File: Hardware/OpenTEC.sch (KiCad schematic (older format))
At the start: 52 parts

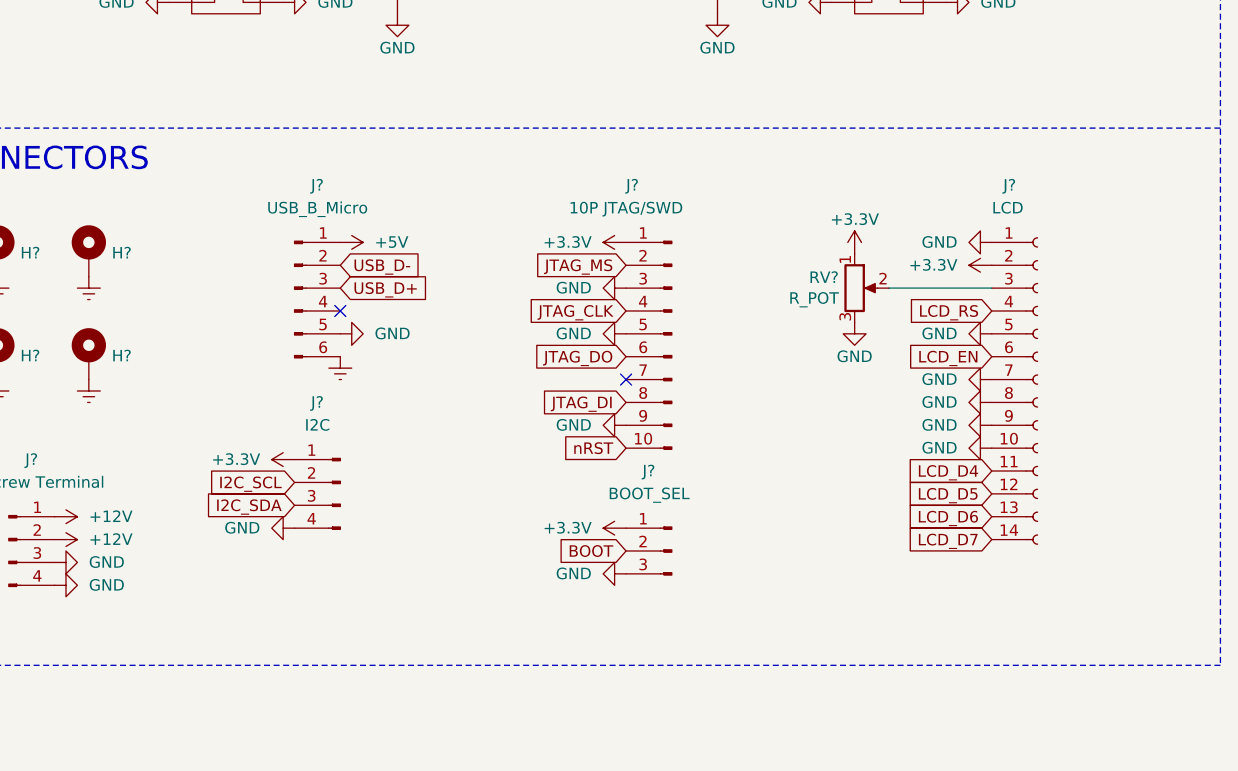
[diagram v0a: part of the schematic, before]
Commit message: Add temperature sensor connectors
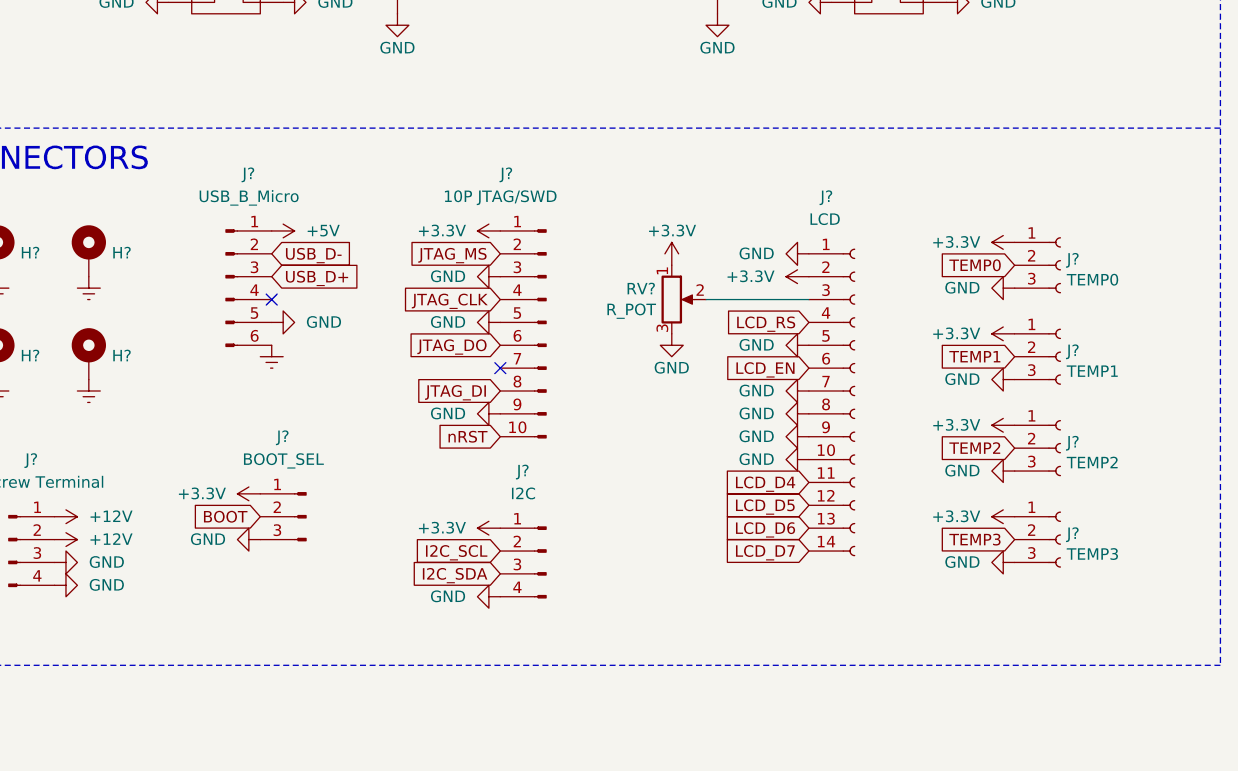
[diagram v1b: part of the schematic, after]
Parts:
- added J?: TEMP0, symbol Connector:Conn_01x03_Female
- added J?: TEMP1, symbol Connector:Conn_01x03_Female
- added J?: TEMP2, symbol Connector:Conn_01x03_Female
- added J?: TEMP3, symbol Connector:Conn_01x03_Female
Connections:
- net +3V3: now also J?.1 (Pin_1), J?.1 (Pin_1), J?.1 (Pin_1), J?.1 (Pin_1)
- net GND: now also J?.3 (Pin_3), J?.3 (Pin_3), J?.3 (Pin_3), J?.3 (Pin_3)
- net TEMP0: now also J?.2 (Pin_2)
- net TEMP1: now also J?.2 (Pin_2)
- net TEMP2: now also J?.2 (Pin_2)
- net TEMP3: now also J?.2 (Pin_2)
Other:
- moved on the sheet: J?, RV?

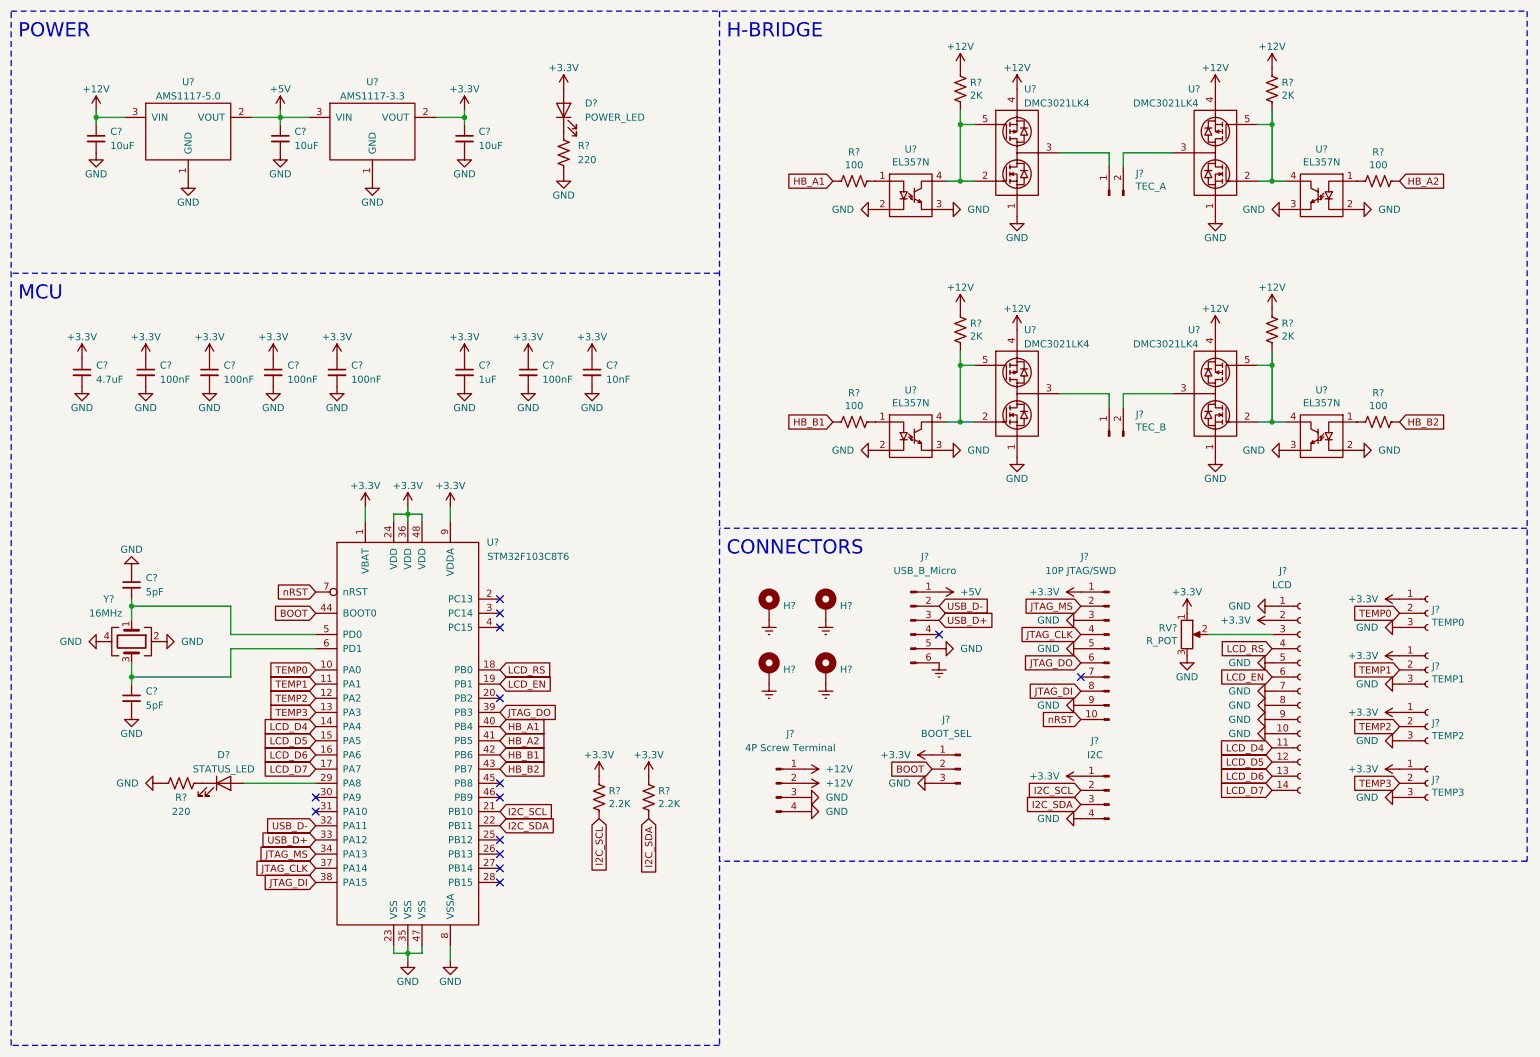
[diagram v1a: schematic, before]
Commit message: Add fan headers
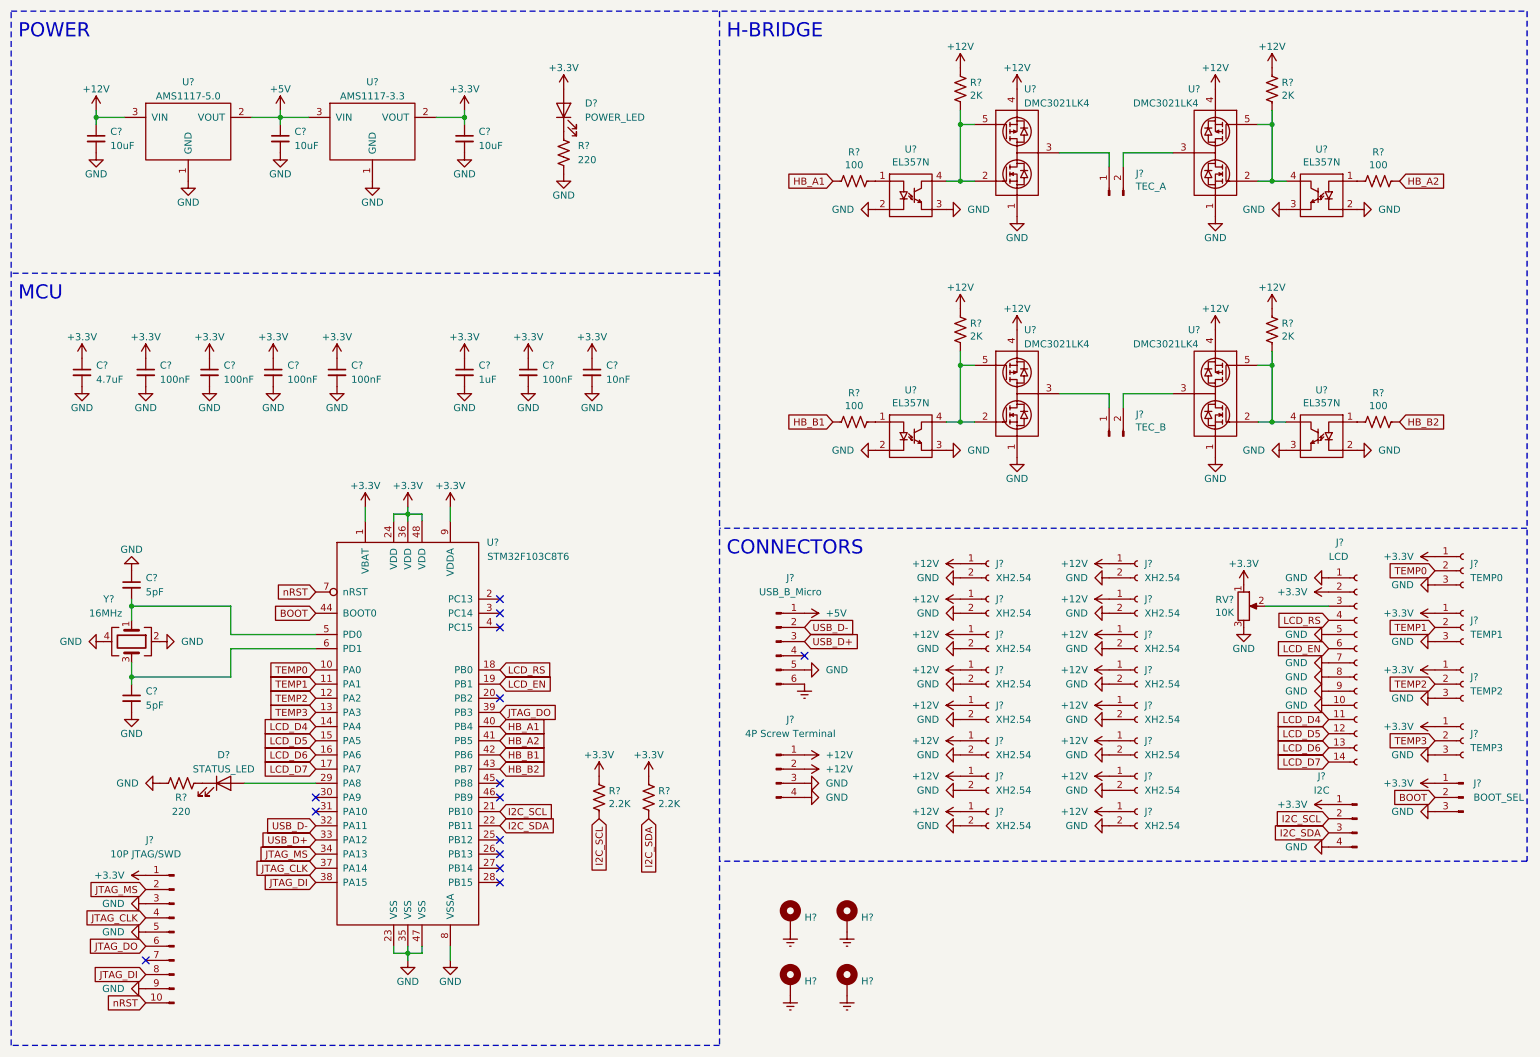
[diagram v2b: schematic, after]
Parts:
- added J? (x16): XH2.54, symbol Connector:Conn_01x02_Female
- RV?: value R_POT -> 10K
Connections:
- net +12V: now also J?.1 (Pin_1), J?.1 (Pin_1), J?.1 (Pin_1), J?.1 (Pin_1), J?.1 (Pin_1), J?.1 (Pin_1), J?.1 (Pin_1), J?.1 (Pin_1), J?.1 (Pin_1), J?.1 (Pin_1), J?.1 (Pin_1), J?.1 (Pin_1), J?.1 (Pin_1), J?.1 (Pin_1), J?.1 (Pin_1), J?.1 (Pin_1)
- net GND: now also J?.2 (Pin_2), J?.2 (Pin_2), J?.2 (Pin_2), J?.2 (Pin_2), J?.2 (Pin_2), J?.2 (Pin_2), J?.2 (Pin_2), J?.2 (Pin_2), J?.2 (Pin_2), J?.2 (Pin_2), J?.2 (Pin_2), J?.2 (Pin_2), J?.2 (Pin_2), J?.2 (Pin_2), J?.2 (Pin_2), J?.2 (Pin_2)
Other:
- moved on the sheet: H?, J?, RV?

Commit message: Add footprints to components
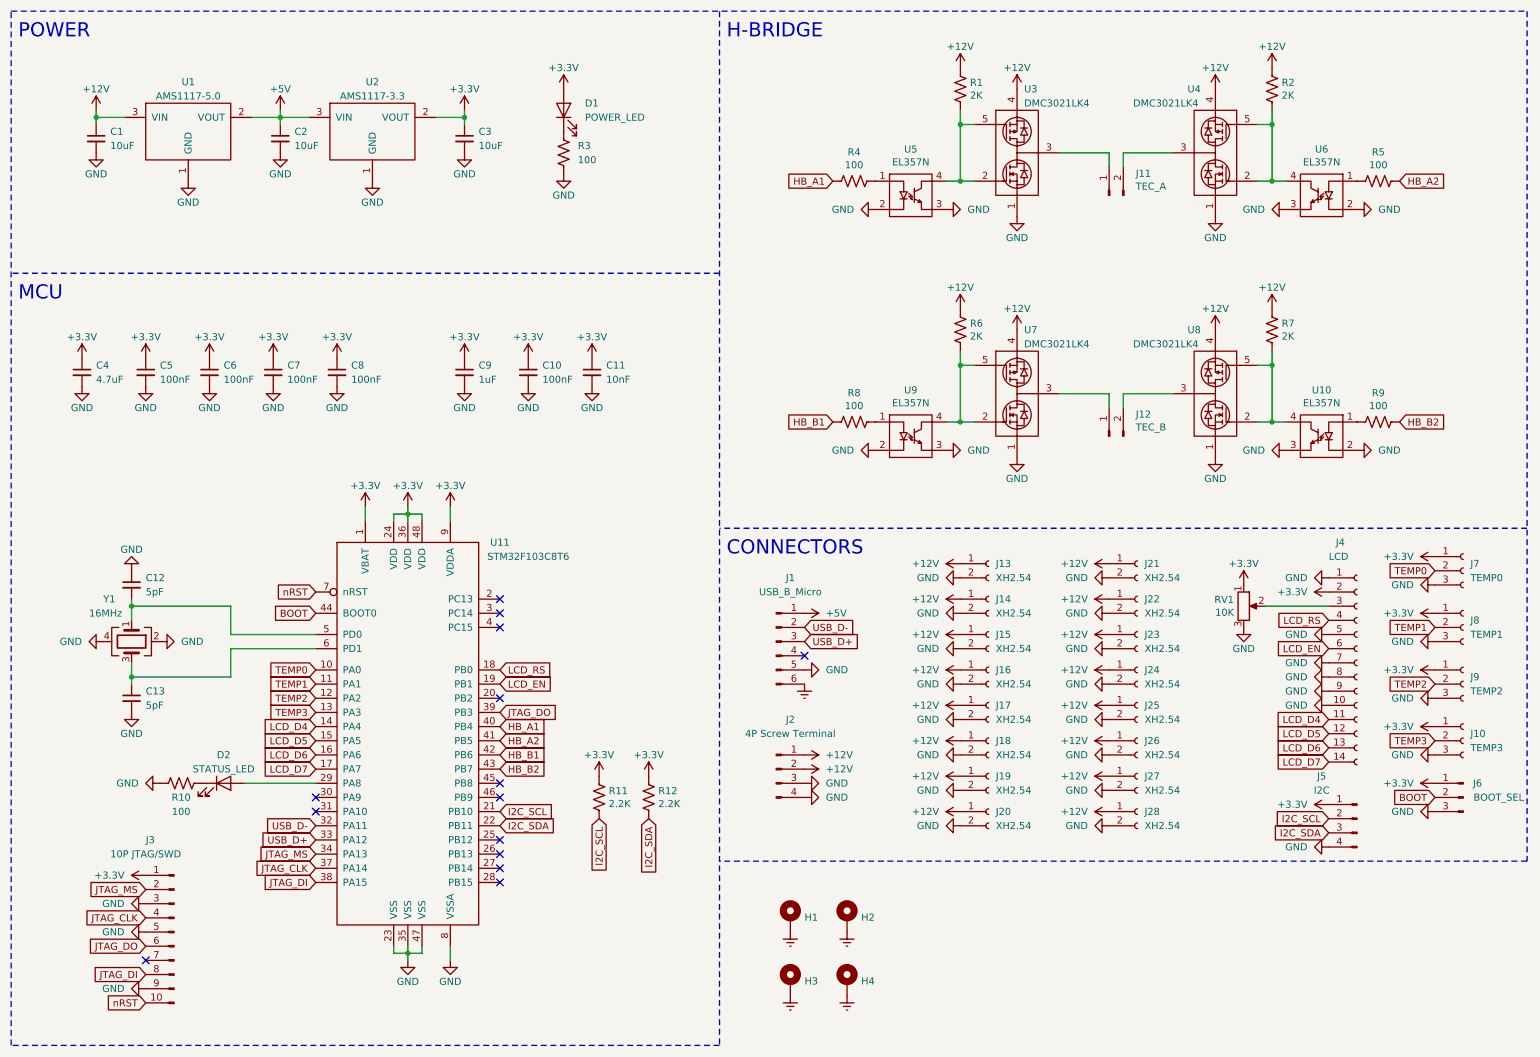
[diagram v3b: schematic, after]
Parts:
- C1, C2, C3, C4, C9: renamed from C?; footprint (none) -> Capacitor_SMD:C_0805_2012Metric
- C10, C11, C5, C6, C7, C8: renamed from C?; footprint (none) -> Capacitor_SMD:C_0402_1005Metric
- C12, C13: renamed from C?; footprint (none) -> Capacitor_SMD:C_0603_1608Metric
- D1, D2: renamed from D?; footprint (none) -> LED_SMD:LED_0603_1608Metric
- H1, H2, H3, H4: renamed from H?; footprint (none) -> MountingHole:MountingHole_3.2mm_M3_Pad_Via
- J1: renamed from J?; footprint (none) -> Connector_USB:USB_Micro-B_GCT_USB3076-30-A
- J10, J7, J8, J9: renamed from J?; footprint (none) -> Connector_PinSocket_2.54mm:PinSocket_1x03_P2.54mm_Vertical
- J11, J12: renamed from J?; footprint (none) -> TerminalBlock:TerminalBlock_bornier-2_P5.08mm
- J13, J14, J15, J16, J17, J18, J19, J20, J21, J22, J23, J24, J25, J26, J27, J28: renamed from J?; footprint (none) -> Connector_JST:JST_XH_B2B-XH-A_1x02_P2.50mm_Vertical
- J2: renamed from J?; footprint (none) -> TerminalBlock:TerminalBlock_bornier-4_P5.08mm
- J3: renamed from J?; footprint (none) -> Connector_PinHeader_2.54mm:PinHeader_2x05_P2.54mm_Vertical
- J4: renamed from J?; footprint (none) -> Connector_PinHeader_2.54mm:PinHeader_1x14_P2.54mm_Vertical
- J5: renamed from J?; footprint (none) -> Connector_PinHeader_2.54mm:PinHeader_1x04_P2.54mm_Vertical
- J6: renamed from J?; footprint (none) -> Connector_PinHeader_2.54mm:PinHeader_1x03_P2.54mm_Vertical
- R10, R3: renamed from R?; value 220 -> 100
- U1, U2: renamed from U?; footprint (none) -> Package_TO_SOT_SMD:SOT-223-3_TabPin2
- U10, U5, U6, U9: renamed from U?; footprint (none) -> Package_SO:SOP-4_3.8x4.1mm_P2.54mm
- U11: renamed from U?; footprint (none) -> Package_QFP:LQFP-48_7x7mm_P0.5mm
- U3, U4, U7, U8: renamed from U?; footprint (none) -> Package_TO_SOT_SMD:TO-252-4
- Y1: renamed from Y?; footprint (none) -> Crystal:Crystal_SMD_3225-4Pin_3.2x2.5mm
- gave numbers to parts that had none: 11

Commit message: Finish PCB layout, export fabrication files
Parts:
- removed J4: LCD, Connector_PinHeader_2.54mm:PinHeader_1x14_P2.54mm_Vertical, symbol Connector:Conn_01x14_Female
- added J4: LCD, Connector_PinSocket_2.54mm:PinSocket_1x16_P2.54mm_Vertical, symbol Connector:Conn_01x16_Female
- C12, C13: value 5pF -> 30pF
- R1, R2, R6, R7: footprint (none) -> Resistor_SMD:R_1206_3216Metric
- R10, R11, R12, R3, R4, R5, R8, R9: footprint (none) -> Resistor_SMD:R_0402_1005Metric
- RV1: footprint (none) -> Potentiometer_THT:Potentiometer_Bourns_3386P_Vertical
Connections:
- net +3V3: now also J4.15 (Pin_15), J4.2 (Pin_2)
- net GND: now also J4.1 (Pin_1), J4.10 (Pin_10), J4.16 (Pin_16), J4.5 (Pin_5), J4.7 (Pin_7), J4.8 (Pin_8), J4.9 (Pin_9)
- net LCD_D4: now also J4.11 (Pin_11)
- net LCD_D5: now also J4.12 (Pin_12)
- net LCD_D6: now also J4.13 (Pin_13)
- net LCD_D7: now also J4.14 (Pin_14)
- net LCD_EN: now also J4.6 (Pin_6)
- net LCD_RS: now also J4.4 (Pin_4)
- net at RV1.2: now also J4.3 (Pin_3)
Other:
- moved on the sheet: J5, RV1

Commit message: Change H-bridge design
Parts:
- removed J11: TEC_A, TerminalBlock:TerminalBlock_bornier-2_P5.08mm, symbol Connector:Conn_01x02_Male
- removed J12: TEC_B, TerminalBlock:TerminalBlock_bornier-2_P5.08mm, symbol Connector:Conn_01x02_Male
- removed R1, R2, R6, R7: 2K, Resistor_SMD:R_1206_3216Metric, symbol Device:R_US
- removed R4, R5, R8, R9: 100, Resistor_SMD:R_0402_1005Metric, symbol Device:R_US
- removed U10, U5, U6, U9: EL357N, Package_SO:SOP-4_3.8x4.1mm_P2.54mm, symbol OpenTEC:EL357N
- removed U3, U4, U7, U8: DMC3021LK4, Package_TO_SOT_SMD:TO-252-4, symbol OpenTEC:DMC3021LK4
- added C14, C15, C16, C17: 10uF, Capacitor_SMD:C_0805_2012Metric, symbol Device:C_Small
- added C18, C19: 1uF, Capacitor_SMD:C_0805_2012Metric, symbol Device:C_Small
- added D3, D4: B5819W, Diode_SMD:D_SOD-123, symbol Device:D_Schottky
- added J11: TEC, TerminalBlock:TerminalBlock_bornier-4_P5.08mm, symbol Connector:Conn_01x04_Male
- added Q1, Q2, Q3, Q4: FDS6574A, Package_SO:SOIC-8_3.9x4.9mm_P1.27mm, symbol OpenTEC:FDS6574A
- added U3, U4: IR2104, Package_SO:SOIC-8_3.9x4.9mm_P1.27mm, symbol OpenTEC:IR2104
- renumbered J28 to J12
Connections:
- net +12V: now also C14.1, C15.1, Q1.5, Q1.6, Q1.7, Q1.8, Q3.5, Q3.6, Q3.7, Q3.8
- net +3V3: now also C16.1, C17.1, D3.2 (A), D4.2 (A), U3.1 (VCC), U4.1 (VCC)
- net GND: now also C14.2, C15.2, C16.2, C17.2, Q2.1, Q2.2, Q2.3, Q4.1, Q4.2, Q4.3, U3.4 (COM), U4.4 (COM)
- net HB_A1 renamed HB1
- net HB1: now also U3.2 (IN)
- net HB_A2 renamed HB1_SD
- net HB1_SD: now also U3.3 (~SD)
- net HB_B1 renamed HB2
- net HB2: now also U4.2 (IN)
- net HB_B2 renamed HB2_SD
- net HB2_SD: now also U4.3 (~SD)
- new net: C18.2, J11.1 (Pin_1), J11.2 (Pin_2), Q1.1, Q1.2, Q1.3, Q2.5, Q2.6, Q2.7, Q2.8, U3.6 (VS)
- new net: Q1.4, U3.7 (HO)
- new net: Q2.4, U3.5 (LO)
- new net: C19.2, J11.3 (Pin_3), J11.4 (Pin_4), Q3.1, Q3.2, Q3.3, Q4.5, Q4.6, Q4.7, Q4.8, U4.6 (VS)
- new net: Q3.4, U4.7 (HO)
- new net: Q4.4, U4.5 (LO)
- new net: C18.1, D3.1 (K), U3.8 (VB)
- new net: C19.1, D4.1 (K), U4.8 (VB)
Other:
- moved on the sheet: J1, J10, J12, J13, J14, J15, J16, J17, J18, J19, J2, J20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

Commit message: Fix USB Micro B connector footprint
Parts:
- J1: footprint Connector_USB:USB_Micro-B_GCT_USB3076-30-A -> Connector_USB:USB_Micro-B_Amphenol_10103594-0001LF_Horizontal
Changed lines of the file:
@@
 F 0 "J1" H 7100 4150 50  0000 C CNN
 F 1 "USB_B_Micro" H 7100 4050 50  0000 C CNN
-F 2 "Connector_USB:USB_Micro-B_GCT_USB3076-30-A" H 7000 3700 50  0001 C CNN
+F 2 "Connector_USB:USB_Micro-B_Amphenol_10103594-0001LF_Horizontal" H 7000 3700 50  0001 C CNN
 F 3 "~" H 7000 3700 50  0001 C CNN
 	1    7000 3700
